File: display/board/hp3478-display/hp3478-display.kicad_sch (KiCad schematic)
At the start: 27 parts, among them J1 SFV10R-1ST, J2 DNP, U1 PIC16F15274-I/MP, U2 DNP

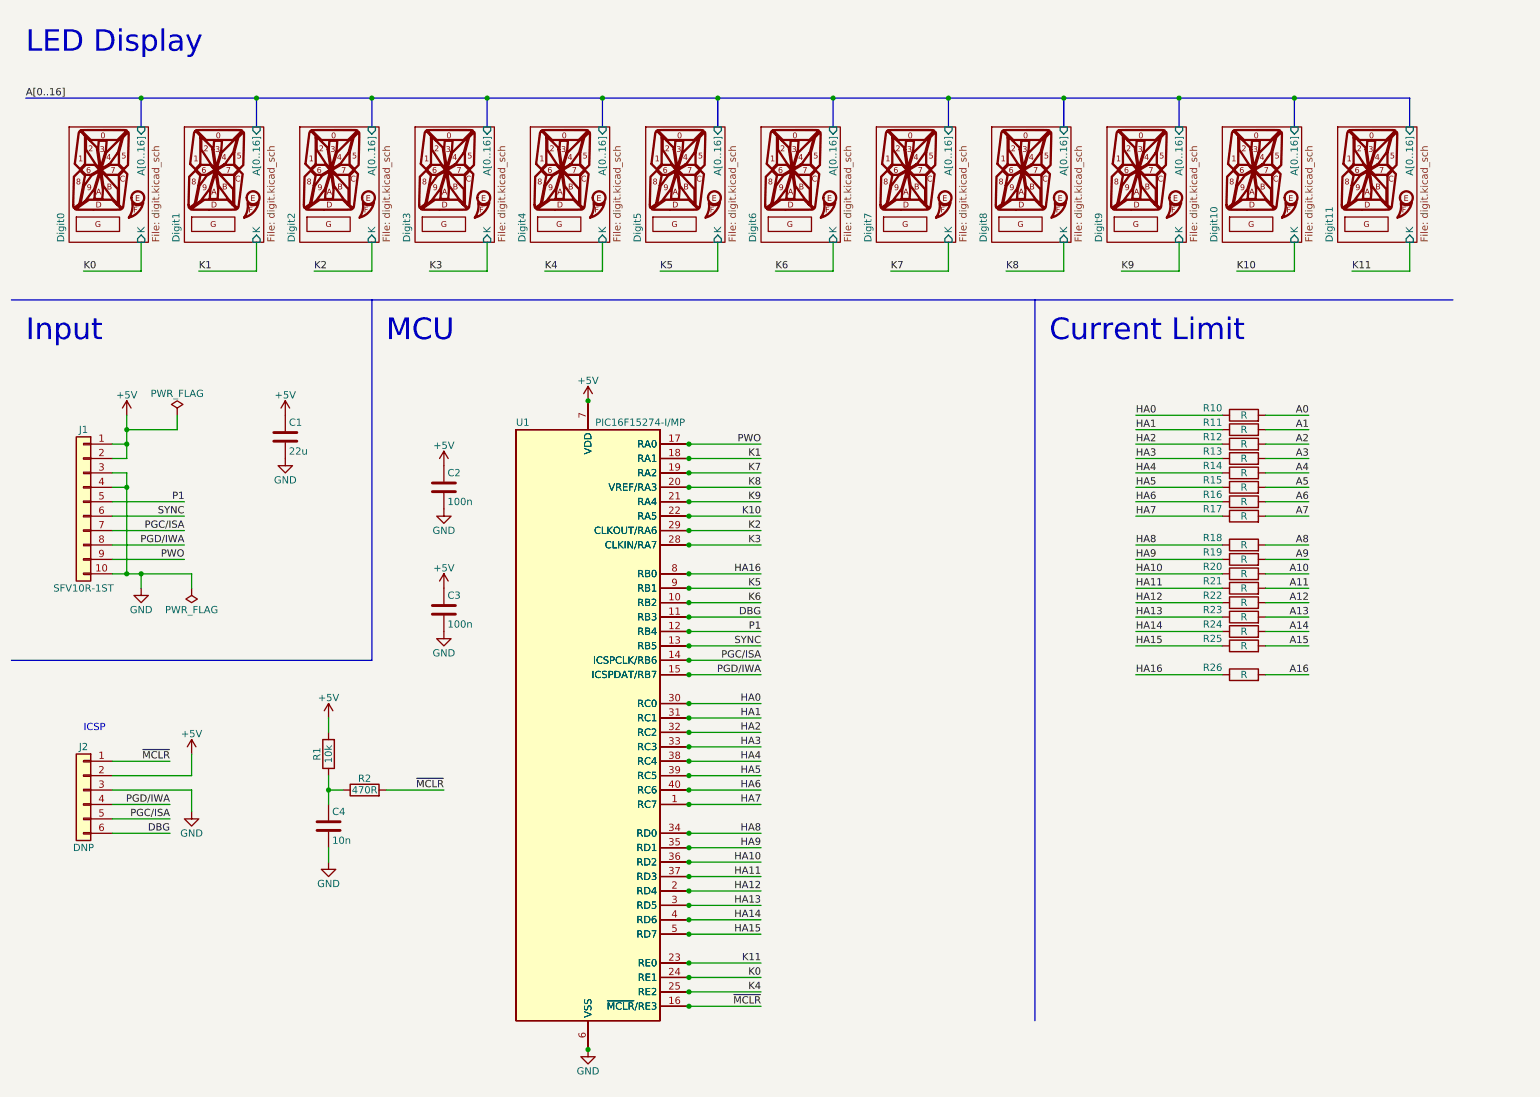
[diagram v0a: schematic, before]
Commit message: Remove MCU and move annunciator LEDs to their own matrix row.
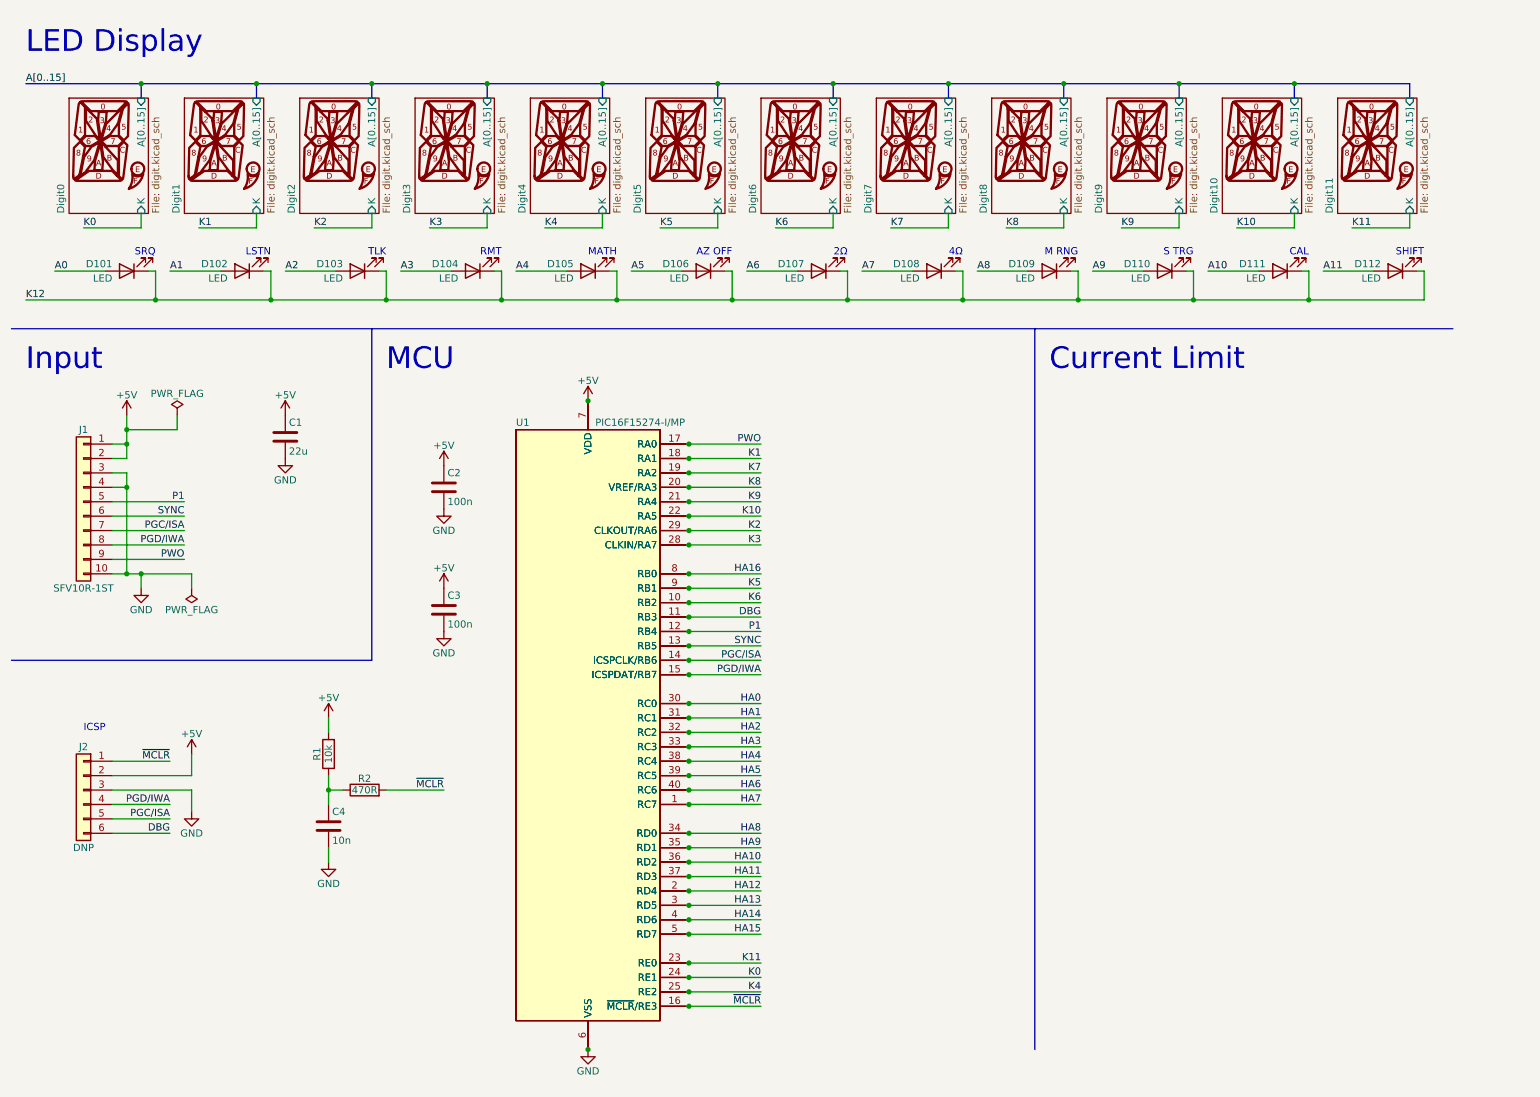
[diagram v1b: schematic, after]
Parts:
- removed R10, R11, R12, R13, R14, R15, R16, R17, R18, R19, R20, R21, R22, R23, R24, R25, R26: R, Resistor_SMD:R_0603_1608Metric, symbol Device:R
- added D101, D102, D103, D104, D105, D106, D107, D108, D109, D110, D111, D112: LED, 0Local:LED_0402_1005Metric, symbol Device:LED
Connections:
- net A0: now also D101.2 (A)
- net A1: now also D102.2 (A)
- net A10: now also D111.2 (A)
- net A11: now also D112.2 (A)
- net A2: now also D103.2 (A)
- net A3: now also D104.2 (A)
- net A4: now also D105.2 (A)
- net A5: now also D106.2 (A)
- net A6: now also D107.2 (A)
- net A7: now also D108.2 (A)
- net A8: now also D109.2 (A)
- net A9: now also D110.2 (A)
- new net K12: D101.1 (K), D102.1 (K), D103.1 (K), D104.1 (K), D105.1 (K), D106.1 (K), D107.1 (K), D108.1 (K), D109.1 (K), D110.1 (K), D111.1 (K), D112.1 (K)
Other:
- sheet Digit0 ports: added A[0..15]; removed A[0..16]
- sheet Digit1 ports: added A[0..15]; removed A[0..16]
- sheet Digit10 ports: added A[0..15]; removed A[0..16]
- sheet Digit11 ports: added A[0..15]; removed A[0..16]
- sheet Digit2 ports: added A[0..15]; removed A[0..16]
- sheet Digit3 ports: added A[0..15]; removed A[0..16]
- sheet Digit4 ports: added A[0..15]; removed A[0..16]
- sheet Digit5 ports: added A[0..15]; removed A[0..16]
- sheet Digit6 ports: added A[0..15]; removed A[0..16]
- sheet Digit7 ports: added A[0..15]; removed A[0..16]
- sheet Digit8 ports: added A[0..15]; removed A[0..16]
- sheet Digit9 ports: added A[0..15]; removed A[0..16]
- note added: "2Ω"
- note added: "4Ω"
- note added: "AZ OFF"
- note added: "CAL"
- note added: "LSTN"
- note added: "M RNG"
- note added: "MATH"
- note added: "RMT"
- note added: "S TRG"
- note added: "SHIFT"
- note added: "SRQ"
- note added: "TLK"

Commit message: Swap out MCU and add high-side driver.
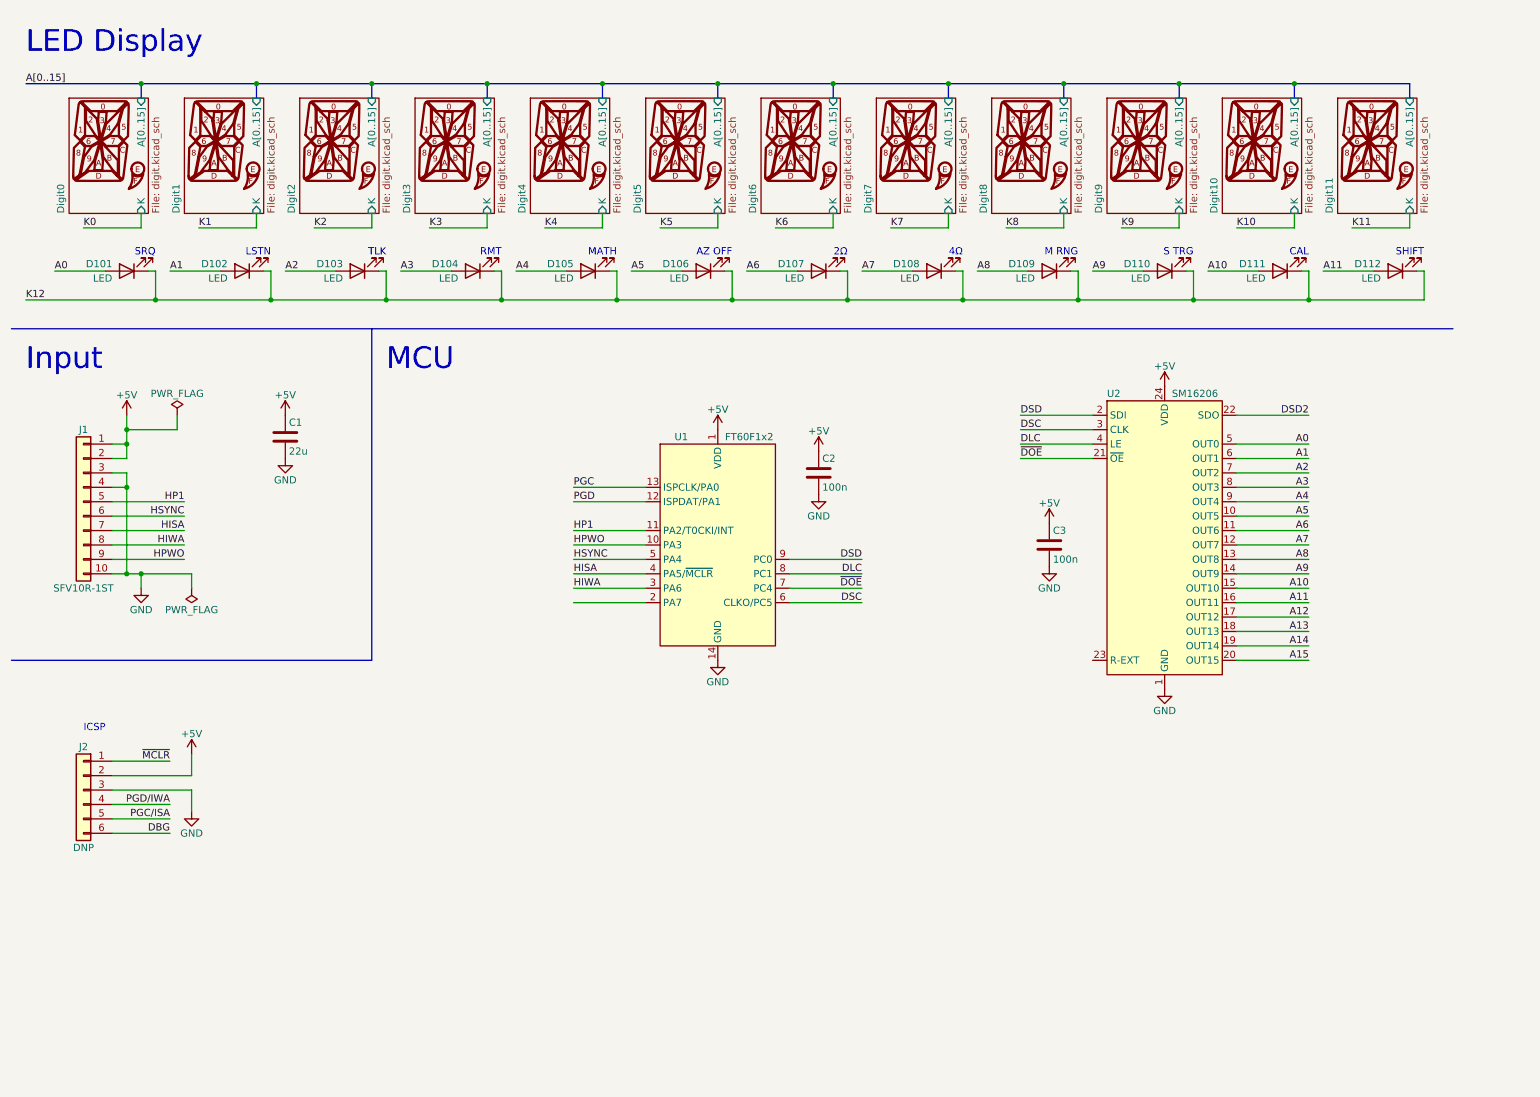
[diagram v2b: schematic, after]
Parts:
- removed C4: 10n, Capacitor_SMD:C_0603_1608Metric, symbol Device:C
- removed R1: 10k, Resistor_SMD:R_0603_1608Metric, symbol Device:R
- removed R2: 470R, Resistor_SMD:R_0603_1608Metric, symbol Device:R
- removed U1: PIC16F15274-I/MP, Package_DFN_QFN:QFN-40-1EP_5x5mm_P0.4mm_EP3.8x3.8mm, symbol 0Local:PIC16F152xx-x_MP
- removed U2: DNP, Package_QFP:TQFP-44_10x10mm_P0.8mm, symbol 0Local:PIC16F152xx-x_PT
- added U1: FT60F1x2, Package_SO:SO-14_3.9x8.65mm_P1.27mm, symbol 0Local:FT60F1x2
- added U2: SM16206, Package_SO:SSOP-24_3.9x8.7mm_P0.635mm, symbol 0Local:SM16206
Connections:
- net +5V: now also U1.1 (VDD), U2.24 (VDD)
- net A0: now also U2.5 (OUT0)
- net A1: now also U2.6 (OUT1)
- net A10: now also U2.15 (OUT10)
- net A11: now also U2.16 (OUT11)
- net A2: now also U2.7 (OUT2)
- net A3: now also U2.8 (OUT3)
- net A4: now also U2.9 (OUT4)
- net A5: now also U2.10 (OUT5)
- net A6: now also U2.11 (OUT6)
- net A7: now also U2.12 (OUT7)
- net A8: now also U2.13 (OUT8)
- net A9: now also U2.14 (OUT9)
- net GND: now also U1.14 (GND), U2.1 (GND)
- net PGC/ISA: no longer J1.7 (Pin_7)
- net PGD/IWA: no longer J1.8 (Pin_8)
- net P1 renamed HP1
- net HP1: now also U1.11 (PA2/T0CKI/INT)
- net PWO renamed HPWO
- net HPWO: now also U1.10 (PA3)
- net SYNC renamed HSYNC
- net HSYNC: now also U1.5 (PA4)
- new net A12: U2.17 (OUT12)
- new net A13: U2.18 (OUT13)
- new net A14: U2.19 (OUT14)
- new net A15: U2.20 (OUT15)
- new net DLC: U1.8 (PC1), U2.4 (LE)
- new net DSC: U1.6 (CLKO/PC5), U2.3 (CLK)
- new net DSD: U1.9 (PC0), U2.2 (SDI)
- new net DSD2: U2.22 (SDO)
- new net HISA: J1.7 (Pin_7), U1.4 (PA5/~{MCLR})
- new net HIWA: J1.8 (Pin_8), U1.3 (PA6)
- new net PGC: U1.13 (ISPCLK/PA0)
- new net PGD: U1.12 (ISPDAT/PA1)
- new net ~{DOE}: U1.7 (PC4), U2.21 (~{OE})
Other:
- note removed: "Current Limit"
- moved on the sheet: C2, C3

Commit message: Add missing colon segment and adjust scan matrix.
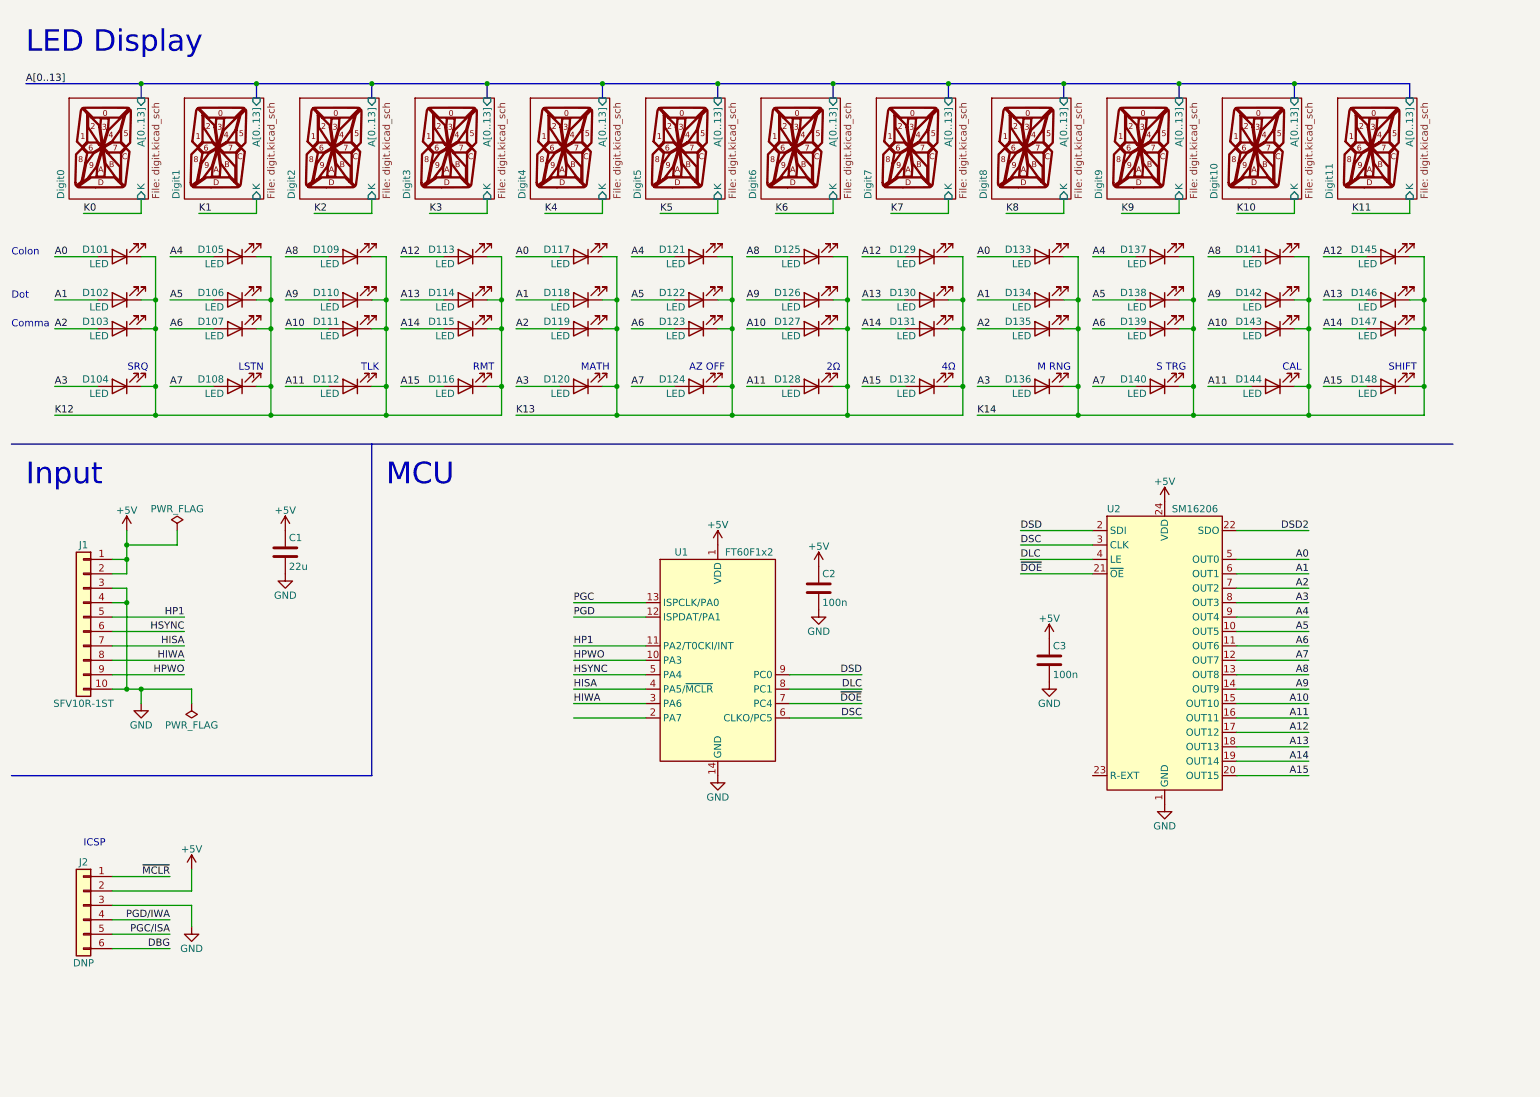
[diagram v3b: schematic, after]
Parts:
- added D101, D102, D103, D105, D106, D107, D109, D110, D111, D113, D114, D115, D117, D118, D119, D121, D122, D123, D125, D126, D127, D129, D130, D131, D133, D134, D135, D137, D138, D139, D141, D142, D143, D145, D146, D147: LED, 0Local:LED_0402_1005Metric, symbol Device:LED
- renumbered D101 to D104, D102 to D108, D103 to D112, D104 to D116, D105 to D120, D106 to D124, D107 to D128, D108 to D132, D109 to D136, D110 to D140, D111 to D144, D112 to D148
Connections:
- net A0: now also D101.2 (A), D117.2 (A), D133.2 (A); no longer D104.2 (A)
- net A1: now also D102.2 (A), D118.2 (A), D134.2 (A); no longer D108.2 (A)
- net A10: now also D111.2 (A), D127.2 (A), D143.2 (A); no longer D144.2 (A)
- net A11: now also D112.2 (A), D128.2 (A), D144.2 (A); no longer D148.2 (A)
- net A12: now also D113.2 (A), D129.2 (A), D145.2 (A)
- net A13: now also D114.2 (A), D130.2 (A), D146.2 (A)
- net A14: now also D115.2 (A), D131.2 (A), D147.2 (A)
- net A15: now also D116.2 (A), D132.2 (A), D148.2 (A)
- net A2: now also D103.2 (A), D119.2 (A), D135.2 (A); no longer D112.2 (A)
- net A3: now also D104.2 (A), D120.2 (A), D136.2 (A); no longer D116.2 (A)
- net A4: now also D105.2 (A), D121.2 (A), D137.2 (A); no longer D120.2 (A)
- net A5: now also D106.2 (A), D122.2 (A), D138.2 (A); no longer D124.2 (A)
- net A6: now also D107.2 (A), D123.2 (A), D139.2 (A); no longer D128.2 (A)
- net A7: now also D108.2 (A), D124.2 (A), D140.2 (A); no longer D132.2 (A)
- net A8: now also D109.2 (A), D125.2 (A), D141.2 (A); no longer D136.2 (A)
- net A9: now also D110.2 (A), D126.2 (A), D142.2 (A); no longer D140.2 (A)
- net K12: now also D101.1 (K), D102.1 (K), D103.1 (K), D105.1 (K), D106.1 (K), D107.1 (K), D109.1 (K), D110.1 (K), D111.1 (K), D113.1 (K), D114.1 (K), D115.1 (K); no longer D120.1 (K), D124.1 (K), D128.1 (K), D132.1 (K), D136.1 (K), D140.1 (K), D144.1 (K), D148.1 (K)
- new net K13: D117.1 (K), D118.1 (K), D119.1 (K), D120.1 (K), D121.1 (K), D122.1 (K), D123.1 (K), D124.1 (K), D125.1 (K), D126.1 (K), D127.1 (K), D128.1 (K), D129.1 (K), D130.1 (K), D131.1 (K), D132.1 (K)
- new net K14: D133.1 (K), D134.1 (K), D135.1 (K), D136.1 (K), D137.1 (K), D138.1 (K), D139.1 (K), D140.1 (K), D141.1 (K), D142.1 (K), D143.1 (K), D144.1 (K), D145.1 (K), D146.1 (K), D147.1 (K), D148.1 (K)
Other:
- sheet Digit0 ports: added A[0..13]; removed A[0..15]
- sheet Digit1 ports: added A[0..13]; removed A[0..15]
- sheet Digit10 ports: added A[0..13]; removed A[0..15]
- sheet Digit11 ports: added A[0..13]; removed A[0..15]
- sheet Digit2 ports: added A[0..13]; removed A[0..15]
- sheet Digit3 ports: added A[0..13]; removed A[0..15]
- sheet Digit4 ports: added A[0..13]; removed A[0..15]
- sheet Digit5 ports: added A[0..13]; removed A[0..15]
- sheet Digit6 ports: added A[0..13]; removed A[0..15]
- sheet Digit7 ports: added A[0..13]; removed A[0..15]
- sheet Digit8 ports: added A[0..13]; removed A[0..15]
- sheet Digit9 ports: added A[0..13]; removed A[0..15]
- note added: "Colon"
- note added: "Comma"
- note added: "Dot"
- moved on the sheet: C1, C2, C3, D104, D108, D112, D116, D120, D124, D128, D132, D136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
